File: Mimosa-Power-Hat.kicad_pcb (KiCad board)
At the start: 2 copper layers, 65 x 56 mm, 76 parts, among them J1 Screw_Terminal_01x04, J2 Screw_Terminal_01x02, J3 40HAT, J4 Screw_Terminal_01x02, J5 Screw_Terminal_01x04, J9 CONN_01X02, M1 Fan_Tacho_PWM, Q1 DMG2305UX, Q2 DMMT5401, U1 ADM3490ExR, U2 CAT24C32, U3 TCAN330, U4 LMZ13608, U5 AB0805, U6 MCP2515-xSO, U7 TXB0102DCU, Y1 32.768 kHz, Y2 8MHz

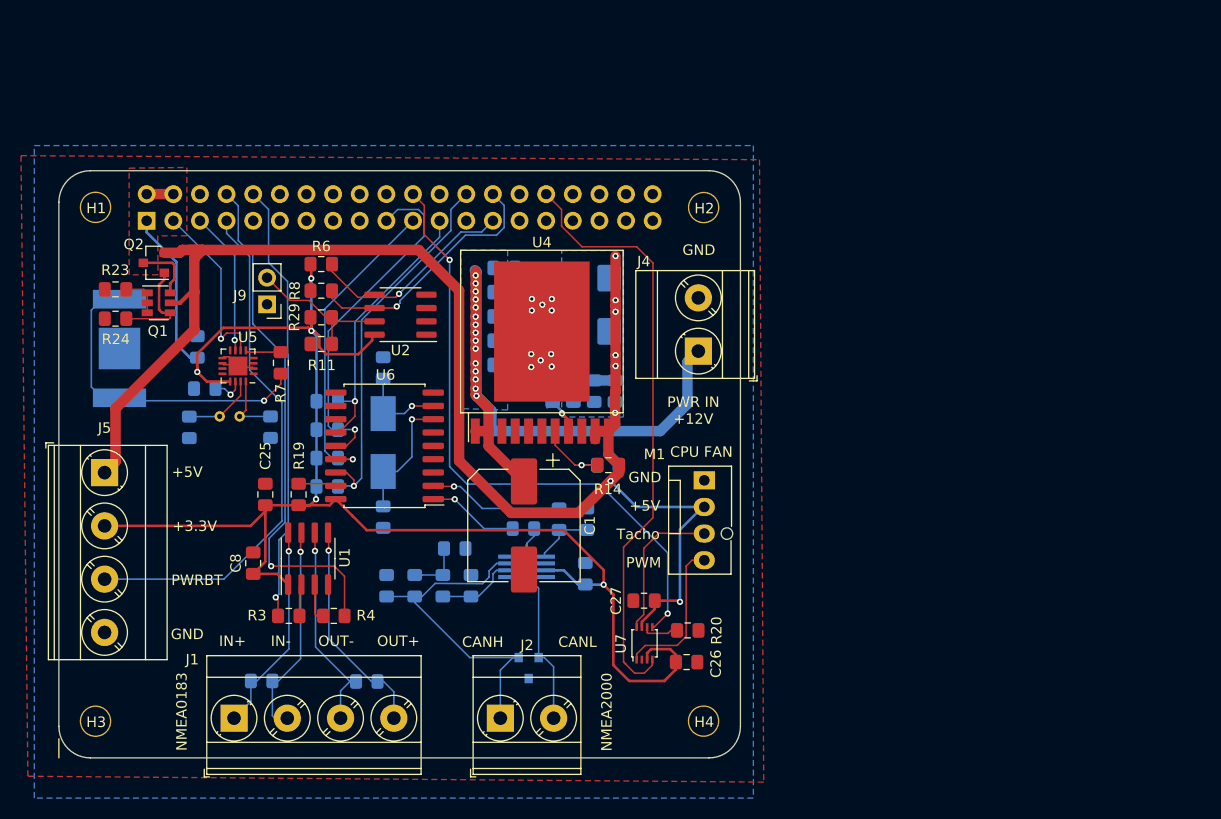
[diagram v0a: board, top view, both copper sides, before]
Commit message: Creation of V1 - correction 1
- Correction of battery holder who was not the proper size
- Changed 12 to 5 DC regulator for a much cheaper one.
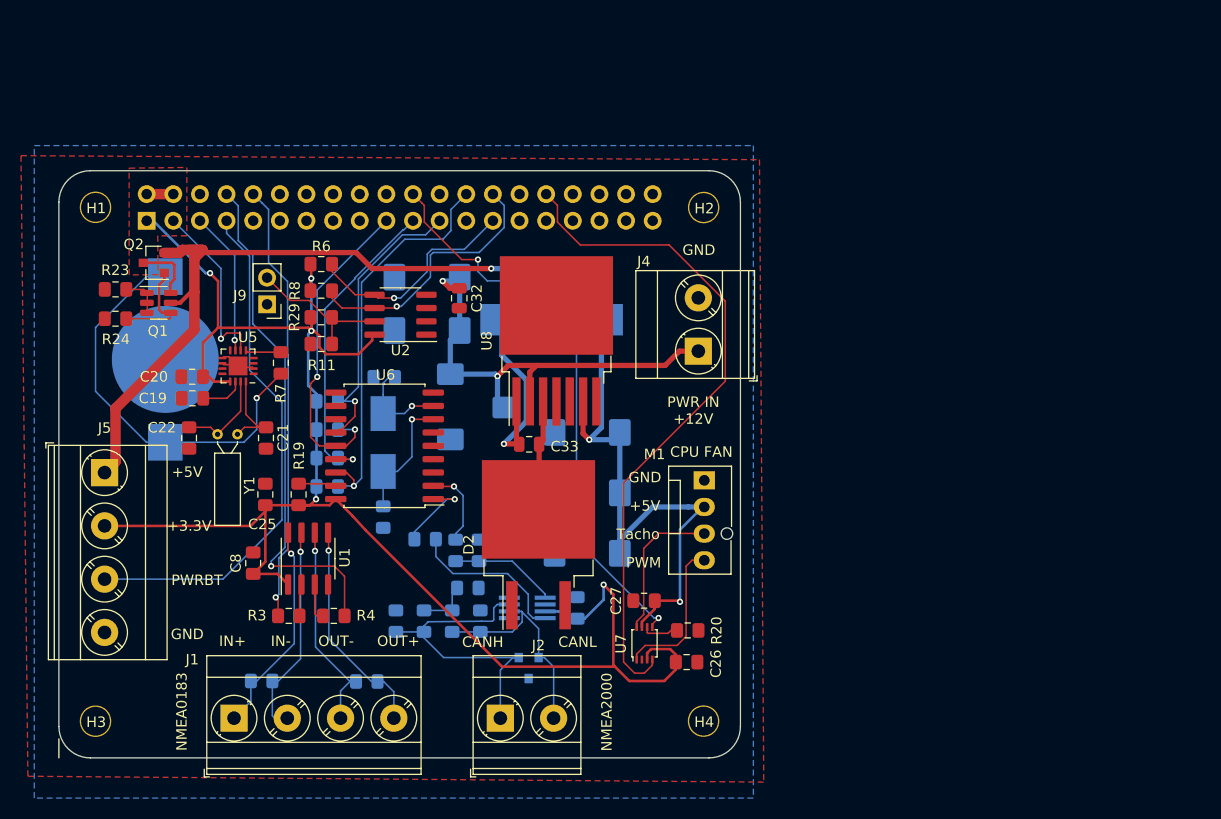
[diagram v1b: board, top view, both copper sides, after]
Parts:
- removed C1: 150uF, Capacitor_SMD:CP_Elec_10x12.5
- removed C10: 470nF, Capacitor_SMD:C_0805_2012Metric_Pad1.15x1.40mm_HandSolder
- removed C14, C15: 330uF, Capacitor_Tantalum_SMD:CP_EIA-7343-31_Kemet-D_Pad2.25x2.55mm_HandSolder
- removed C16: 47uF, Capacitor_SMD:C_0805_2012Metric_Pad1.15x1.40mm_HandSolder
- removed C17, C18, C6, C9: 47nF, Capacitor_SMD:C_0805_2012Metric_Pad1.15x1.40mm_HandSolder
- removed C2, C3, C4: 10uF, Capacitor_SMD:C_0805_2012Metric_Pad1.15x1.40mm_HandSolder
- removed R14: 8k, Resistor_SMD:R_0805_2012Metric_Pad1.15x1.40mm_HandSolder
- removed R15: 1.5k, Resistor_SMD:R_0805_2012Metric_Pad1.15x1.40mm_HandSolder
- removed REF**: OSHW-Logo2_9.8x8mm_SilkScreen, Symbol:OSHW-Logo2_9.8x8mm_SilkScreen
- removed U4: LMZ13608, Package_TO_SOT_SMD:Texas_NDY0011A
- added C28: 10uF, Capacitor_Tantalum_SMD:CP_EIA-7343-31_Kemet-D, B.Cu at (115.9, 83.3)
- added C29: 10uF, Capacitor_Tantalum_SMD:CP_EIA-7343-31_Kemet-D, B.Cu at (121.2, 86.5)
- added C30: 10uF, Capacitor_Tantalum_SMD:CP_EIA-7343-31_Kemet-D, B.Cu at (113.7, 76.1)
- added C31: 10uF, Capacitor_Tantalum_SMD:CP_EIA-7343-31_Kemet-D, B.Cu at (113.7, 71.0)
- added C32: 470nF, Capacitor_SMD:C_0805_2012Metric, F.Cu at (116.7, 73.0)
- added C33: 10nF, Capacitor_SMD:C_0805_2012Metric, F.Cu at (123.4, 86.9)
- added C34: 150uF, Capacitor_Tantalum_SMD:CP_EIA-7343-31_Kemet-D, B.Cu at (128.9, 91.5)
- added C35: 150uF, Capacitor_Tantalum_SMD:CP_EIA-7343-31_Kemet-D, B.Cu at (128.9, 85.8)
- added C36: 150uF, Capacitor_Tantalum_SMD:CP_EIA-7343-31_Kemet-D, B.Cu at (128.9, 97.3)
- added D2: 6TQ045S, Package_TO_SOT_SMD:TO-263-2, F.Cu at (124.3, 96.5)
- added L1: 15uH, Inductor_SMD:L_11.5x10.3_H4mm, B.Cu at (125.5, 75.0)
- added U8: LM2678, Package_TO_SOT_SMD:TO-263-7_TabPin4, F.Cu at (126.0, 77.0)
- BT1: footprint Battery:BatteryHolder_Keystone_2998_1x6.8mm -> Battery:BatteryHolder_Keystone_3000_1x12mm
- C19, C20, C21, C22, Y1: moved to F.Cu
- R7: value TBD -> 1.5k
- moved C5 10.7 mm to (118.6, 97.0)
- moved R1 10.3 mm to (116.4, 97.0)
- moved R2 9.43 mm to (113.5, 96.0)
- moved BT1 4.49 mm to (88.7, 78.8), turned to 90 degrees
- moved C13 3.96 mm to (117.6, 100.6)
- moved U3 3.91 mm to (123.2, 102.5)
- moved C12 3.49 mm to (118.7, 103.8)
- moved C11 3.49 mm to (110.7, 103.8)
- moved R12 3.49 mm to (113.4, 103.8)
- moved R13 3.49 mm to (116.1, 103.8)
- moved C7 3.35 mm to (128.0, 102.5)
- moved C20 2.89 mm to (91.3, 80.5), turned to 0 degrees
- moved Y1 2.71 mm to (93.7, 86.0), turned to 0 degrees
- moved C19 1.49 mm to (91.3, 82.5)
- moved C21 1.12 mm to (98.3, 86.3)
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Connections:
- Y1 pad 1: Net-(C21-Pad2) -> Net-(C22-Pad2)
- Y1 pad 2: Net-(C22-Pad2) -> Net-(C21-Pad2)
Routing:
- net +12V: track 64.9 -> 45.0 mm, vias 15 -> 2
- net Net-(C33-Pad1): track 0.00 -> 19.4 mm, vias 0 -> 1
- net +5V: track 143.7 -> 132.6 mm, vias 8 -> 3
- net Net-(C33-Pad2): track 0.00 -> 10.5 mm
- net GND: track 14.9 -> 5.08 mm, vias 10 -> 0
- net Net-(R2-Pad1): track 6.28 -> 15.6 mm
- net Net-(BT1-Pad1): track 30.7 -> 38.9 mm
- net Net-(R14-Pad2): track 7.66 -> 0.00 mm, vias 1 -> 0
- net /FAN-PWM-(GPIO12): track 57.4 -> 64.7 mm
- net /FAN-RPM-(GPIO24): track 61.5 -> 55.0 mm
- net TX_CAN: track 12.9 -> 7.73 mm
- net Net-(C12-Pad2): track 25.5 -> 21.0 mm
- net Net-(C5-Pad2): track 5.78 -> 10.2 mm
- net Net-(C10-Pad1): track 4.27 -> 0.00 mm, vias 1 -> 0
- net /SPI-MOSI-(GPIO10): track 33.8 -> 30.9 mm, vias 1 -> 2
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- removed copper zone on B.Cu, net +12V
- removed copper zone on B.Cu, net +5V
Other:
- board text added: "Mimosa - Power Hat - V1 Designed by Jérôme Béguin 11.2020"
- board text removed: "Mimosa - Power Hat - V0 Designed by Jérôme Béguin 08.2020"

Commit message: Correction of NMEA2000 RX/TX inversion, addition of seatalk circuit connection (not yet routed)
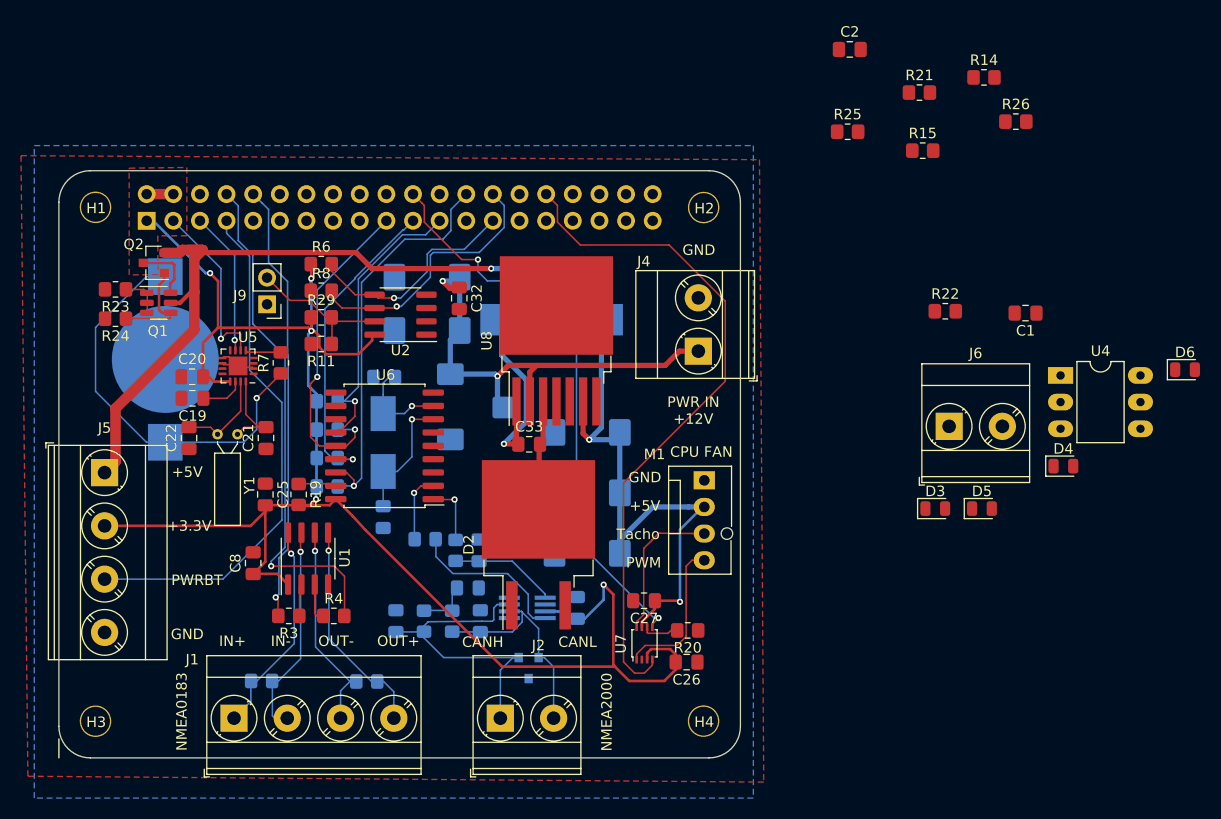
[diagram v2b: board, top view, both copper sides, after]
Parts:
- removed G***: LOGO, project_footprints:Mimosa-Logo
- added C1: C, Capacitor_SMD:C_0805_2012Metric_Pad1.18x1.45mm_HandSolder, F.Cu at (170.7, 74.4)
- added C2: 100nF, Capacitor_SMD:C_0805_2012Metric_Pad1.18x1.45mm_HandSolder, F.Cu at (154.0, 49.3)
- added D3: LED, LED_SMD:LED_0805_2012Metric, F.Cu at (162.1, 93.0)
- added D4: LED, LED_SMD:LED_0805_2012Metric, F.Cu at (174.3, 89.0)
- added D5: LED, LED_SMD:LED_0805_2012Metric, F.Cu at (166.6, 93.0)
- added D6: LED, LED_SMD:LED_0805_2012Metric, F.Cu at (185.9, 79.8)
- added J6: Screw_Terminal_01x02, TerminalBlock_Phoenix:TerminalBlock_Phoenix_MKDS-3-2-5.08_1x02_P5.08mm_Horizontal, F.Cu at (163.4, 85.2)
- added R14: 1.2k, Resistor_SMD:R_0805_2012Metric_Pad1.20x1.40mm_HandSolder, F.Cu at (166.8, 51.9)
- added R15: 1.2k, Resistor_SMD:R_0805_2012Metric_Pad1.20x1.40mm_HandSolder, F.Cu at (160.9, 58.9)
- added R21: 1.2k, Resistor_SMD:R_0805_2012Metric_Pad1.20x1.40mm_HandSolder, F.Cu at (160.6, 53.4)
- added R22: 1.2k, Resistor_SMD:R_0805_2012Metric_Pad1.20x1.40mm_HandSolder, F.Cu at (163.1, 74.2)
- added R25: 250R, Resistor_SMD:R_0805_2012Metric_Pad1.20x1.40mm_HandSolder, F.Cu at (153.8, 57.1)
- added R26: 1.2k, Resistor_SMD:R_0805_2012Metric_Pad1.20x1.40mm_HandSolder, F.Cu at (169.8, 56.1)
- added U4: H11L1, Package_DIP:DIP-6_W7.62mm_LongPads, F.Cu at (174.1, 80.3)
- C11, C12, C13, C19, C20, C21, C22, C23, C24, C25, C26, C27, C5, C7, C8: footprint Capacitor_SMD:C_0805_2012Metric_Pad1.15x1.40mm_HandSolder -> Capacitor_SMD:C_0805_2012Metric_Pad1.18x1.45mm_HandSolder
- C32, C33: footprint Capacitor_SMD:C_0805_2012Metric -> Capacitor_SMD:C_0805_2012Metric_Pad1.18x1.45mm_HandSolder
- R1, R10, R11, R12, R13, R16, R17, R18, R19, R2, R20, R23, R24, R29, R3, R4, R5, R6, R7, R8, R9: footprint Resistor_SMD:R_0805_2012Metric_Pad1.15x1.40mm_HandSolder -> Resistor_SMD:R_0805_2012Metric_Pad1.20x1.40mm_HandSolder
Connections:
- J3 pad 33: (no net) -> /CLK-OUT
- J3 pad 37: (no net) -> /SeaTalk1
- R1 pad 2: TX_CAN -> RX_CAN
- R2 pad 2: RX_CAN -> TX_CAN
- U6 pad 3: (no net) -> /CLK-OUT
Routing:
- net RX_CAN: track 7.91 -> 5.93 mm
- net TX_CAN: track 7.73 -> 6.54 mm

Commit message: add connection for seatalk, cleaned board and schematic
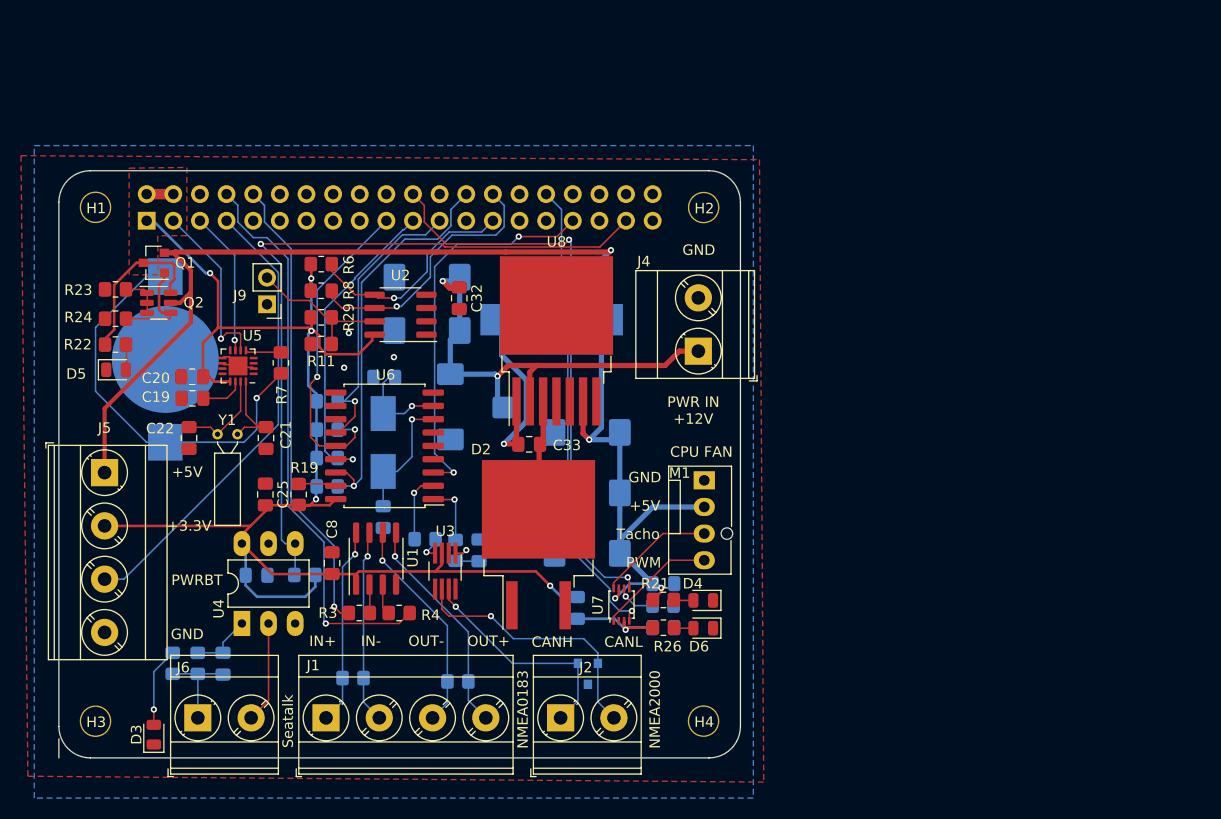
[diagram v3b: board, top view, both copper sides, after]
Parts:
- removed C11, C12, C13: C, Capacitor_SMD:C_0805_2012Metric_Pad1.18x1.45mm_HandSolder
- removed R12, R13: 60R, Resistor_SMD:R_0805_2012Metric_Pad1.20x1.40mm_HandSolder
- C1: value C -> DNP; moved to B.Cu
- C2, C26, C27, R14, R15, R20, R25: moved to B.Cu
- C21, C22: value nc -> 18pF
- C5: value C -> DNP
- R1, R2, R3, R4: value R -> 0R
- R10, R5: value R_Small -> DNP
- R23, R29: value 10K -> 10k
- R24: value 47K -> 47k
- R6, R8: value 3.9K -> 3.9k
- R9: value NC -> DNP
- U3: moved to F.Cu
- moved R14 95.4 mm to (89.4, 107.8), turned to 270 degrees
- moved R15 84.7 mm to (91.8, 107.8), turned to 270 degrees
- moved D5 83.6 mm to (84.0, 79.8)
- moved C1 83.5 mm to (94.2, 107.8), turned to 270 degrees
- moved U4 81.6 mm to (96.0, 104.0), turned to 90 degrees
- moved R22 79.2 mm to (83.9, 77.4), turned to 180 degrees
- moved D3 77.6 mm to (87.6, 114.6), turned to 90 degrees
- moved J6 76.9 mm to (91.8, 113.0)
- moved C2 75.6 mm to (97.4, 99.4), turned to 180 degrees
- moved R25 66.8 mm to (102.0, 99.4)
- moved R26 58.8 mm to (136.2, 104.4), turned to 180 degrees
- moved R21 54.2 mm to (136.2, 101.8), turned to 180 degrees
- moved D6 52.1 mm to (140.0, 104.4), turned to 180 degrees
- moved D4 36.7 mm to (140.0, 101.8), turned to 180 degrees
- moved J1 8.78 mm to (104.0, 113.0)
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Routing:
- net /SeaTalk1: track 0.00 -> 69.5 mm, vias 0 -> 1
- net /CLK-OUT: track 0.00 -> 37.3 mm, vias 0 -> 2
- net /FAN-PWM-(GPIO12): track 64.7 -> 44.9 mm, vias 0 -> 1
- net Net-(R2-Pad1): track 15.6 -> 2.47 mm, vias 0 -> 1
- net ST-GND: track 0.00 -> 9.69 mm
- net /P5V: track 8.52 -> 17.6 mm
- net ST-Data: track 0.00 -> 9.03 mm
- net Net-(D1-Pad1): track 30.2 -> 21.7 mm, vias 0 -> 1
- net Net-(D3-Pad2): track 0.00 -> 7.61 mm, vias 0 -> 1
- net +3V3: track 161.7 -> 155.6 mm, vias 5 -> 6
- net Net-(C1-Pad1): track 0.00 -> 5.96 mm
- net /Power-Button-(GPIO4): track 50.0 -> 44.2 mm
- net Net-(C13-Pad2): track 5.18 -> 0.00 mm
- net Net-(C5-Pad2): track 10.2 -> 5.53 mm, vias 0 -> 1
- net RX_NMEA183: track 49.5 -> 54.0 mm
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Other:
- board text added: "Open Reef - Power & Com Shield V1 Designed by Jérôme Béguin 04.2021"
- board text added: "Seatalk"
- board text removed: "Mimosa - Power Hat - V1 Designed by Jérôme Béguin 11.2020"

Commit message: New branch V2, update to kicad V6, Version of the board will add Attiny microcontroller for safe shutdown and watchdog.
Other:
- net class Default removed
- net class Power removed
